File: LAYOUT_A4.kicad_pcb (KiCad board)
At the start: 2 copper layers, 209.6 x 205.7 mm, 108 parts, among them SW1 DPST, SW10 DPST, SW11 DPST, SW12 DPST, SW13 DPST, SW14 DPST, SW15 DPST, SW16 DPST, SW2 DPST, SW3 DPST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

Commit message: New A4 Layout
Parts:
- moved COLS1 160.2 mm to (174.0, 133.3)
- moved ROWS1 160.2 mm to (174.0, 120.7)
- moved C10 158.1 mm to (100.3, 146.1)
- moved C11 158.1 mm to (99.1, 170.2)
- moved C12 158.1 mm to (99.1, 236.2)
- moved C13 158.1 mm to (123.2, 146.1)
- moved C3 158.1 mm to (30.5, 236.2)
- moved C4 158.1 mm to (54.6, 146.1)
- moved C8 158.1 mm to (76.2, 170.2)
- moved C9 158.1 mm to (76.2, 236.2)
- moved COLS2 158.1 mm to (175.3, 172.7)
- moved D13 158.1 mm to (170.2, 257.8)
- moved D14 158.1 mm to (143.5, 261.6)
- moved D16 158.1 mm to (97.8, 261.6)
- moved D19 158.1 mm to (30.5, 229.9)
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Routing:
- net GND: track 0.00 -> 535.3 mm
- net /c1: track 0.00 -> 285.1 mm, vias 0 -> 1
- net /c2: track 0.00 -> 272.8 mm, vias 0 -> 2
- net /c4: track 0.00 -> 270.2 mm, vias 0 -> 3
- net /col2: track 0.00 -> 269.2 mm, vias 0 -> 4
- net /c3: track 0.00 -> 264.4 mm, vias 0 -> 3
- net /col1: track 0.00 -> 252.9 mm, vias 0 -> 2
- net /a4: track 0.00 -> 217.4 mm, vias 0 -> 1
- net /col3: track 0.00 -> 205.0 mm, vias 0 -> 2
- net /row3: track 0.00 -> 190.7 mm, vias 0 -> 2
- net /row1: track 0.00 -> 186.8 mm
- net /row2: track 0.00 -> 186.3 mm, vias 0 -> 1
- net /col4: track 0.00 -> 177.3 mm, vias 0 -> 2
- net /a1: track 0.00 -> 160.9 mm
- net /col5: track 0.00 -> 145.2 mm, vias 0 -> 2
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
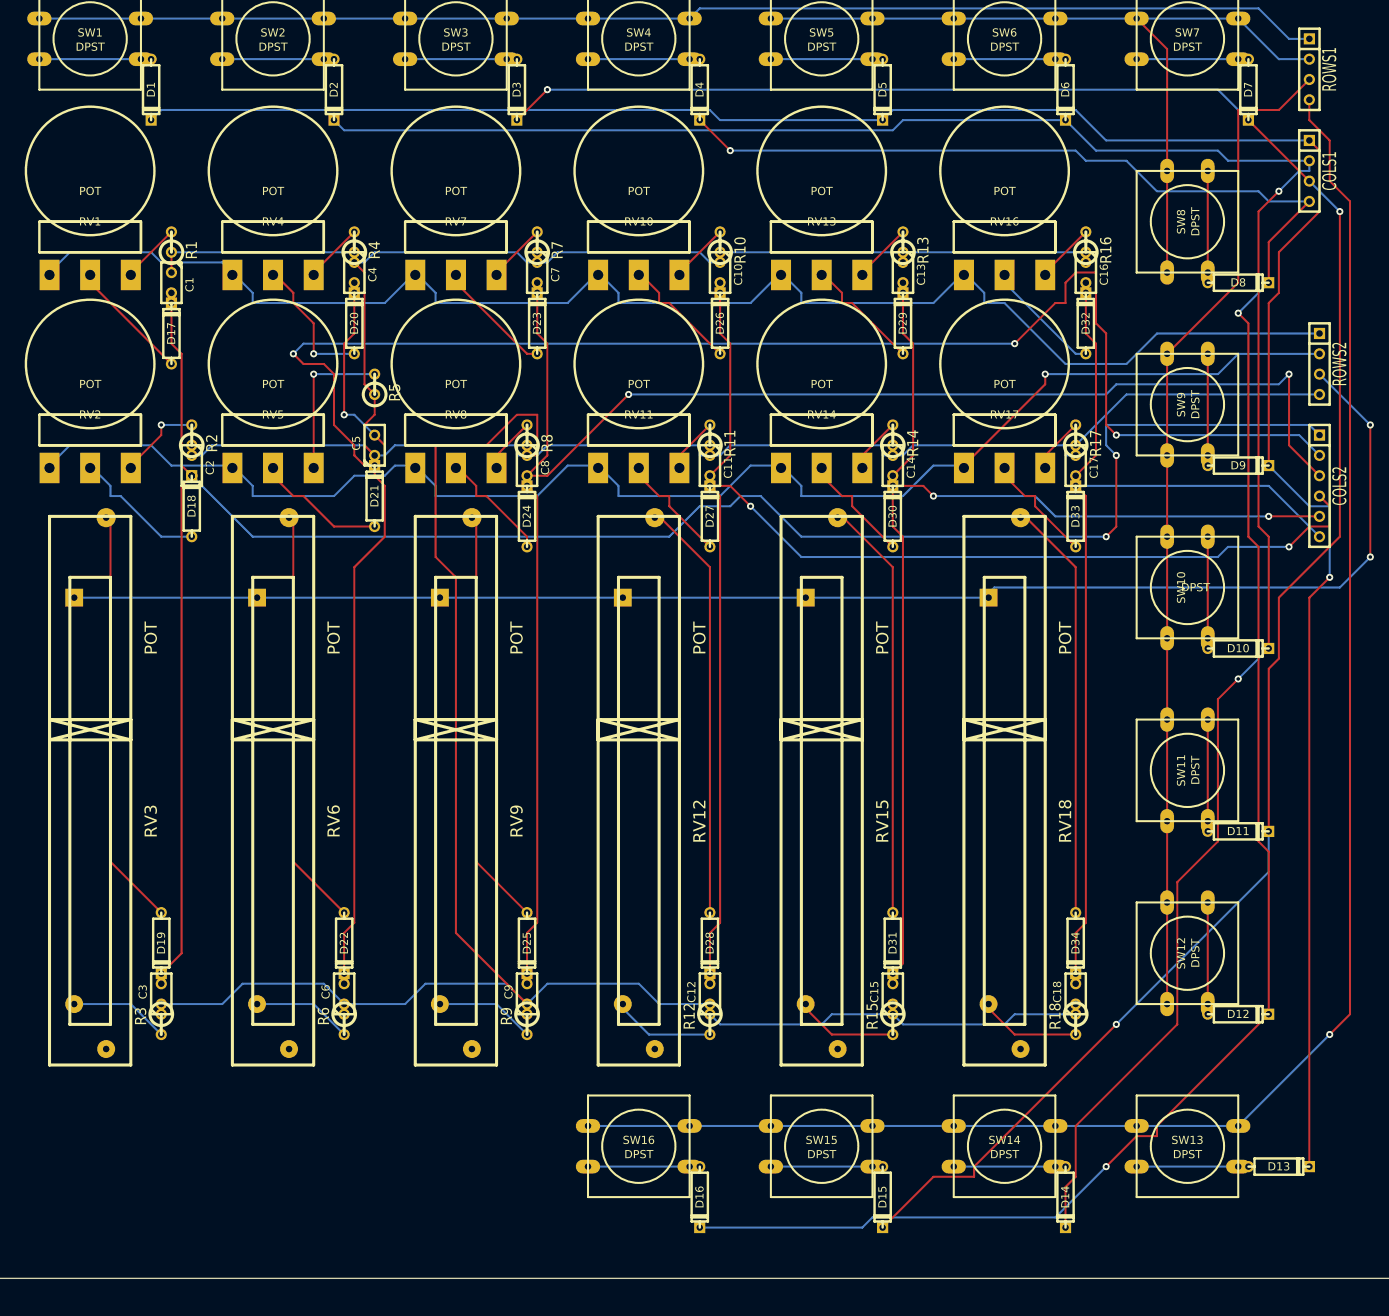
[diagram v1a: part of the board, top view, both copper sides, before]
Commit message: MIDI I/O added
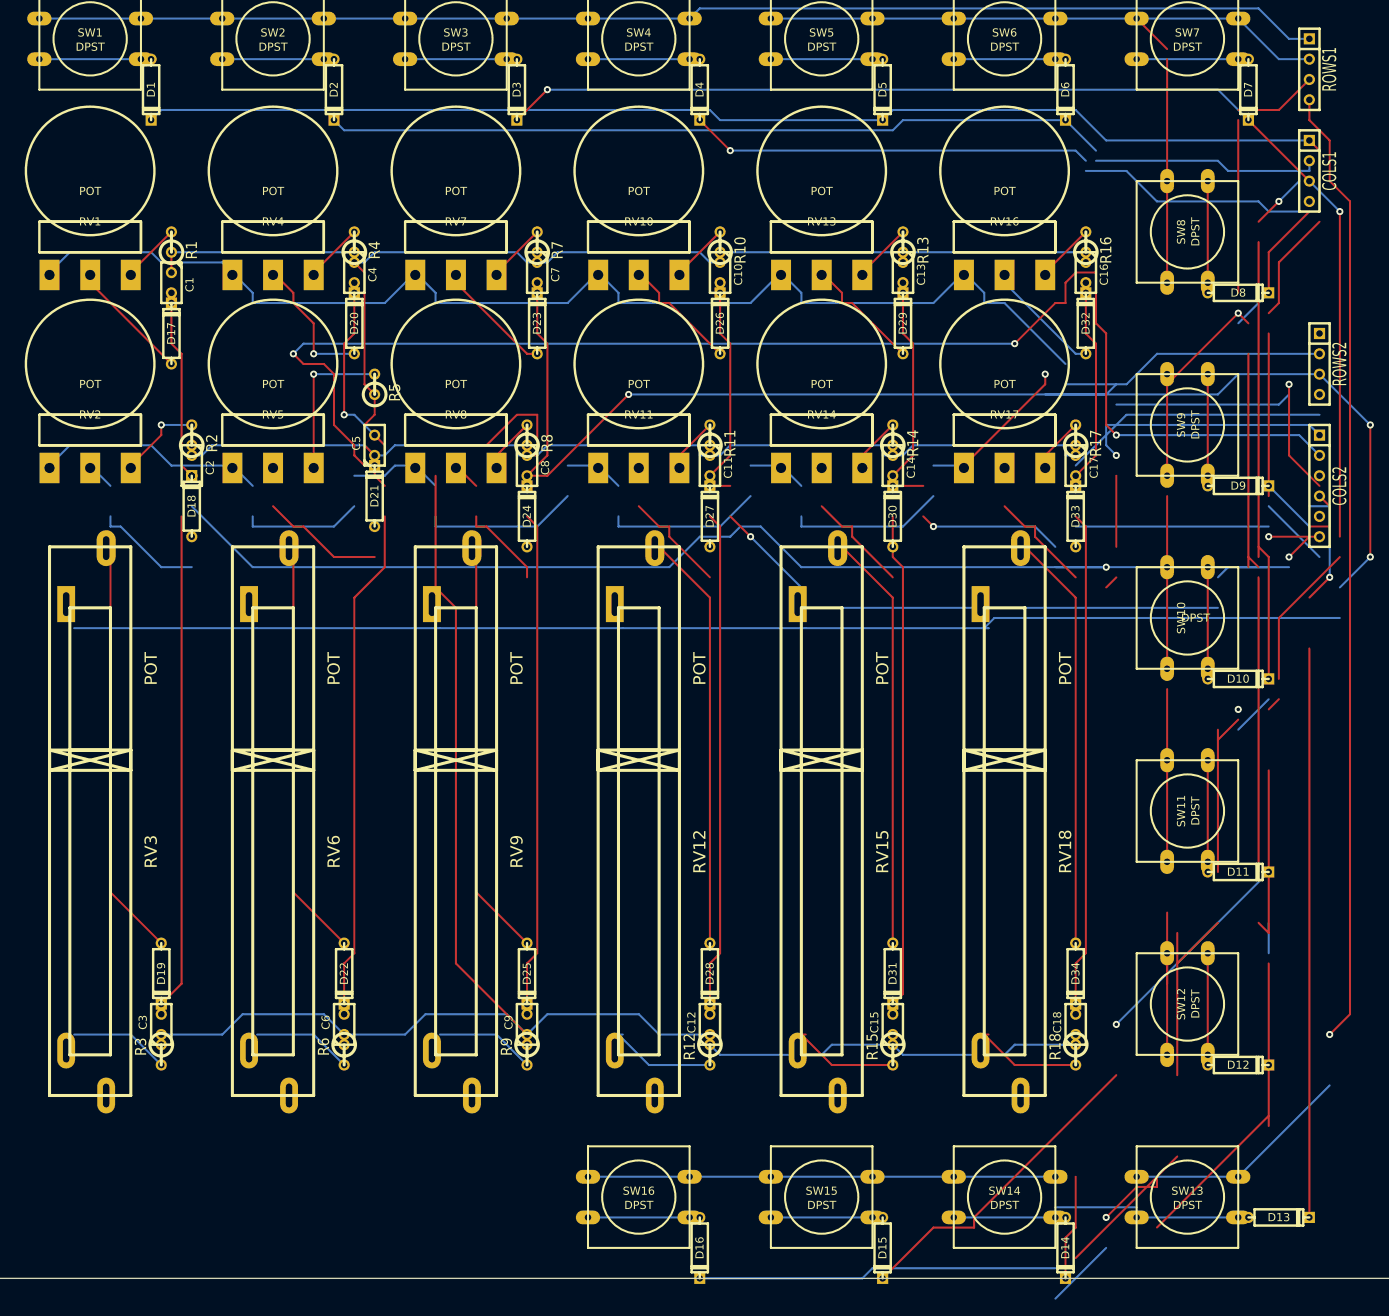
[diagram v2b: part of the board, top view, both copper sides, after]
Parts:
- moved D12 6.35 mm to (165.1, 245.1)
- moved D13 6.35 mm to (170.2, 264.2)
- moved D14 6.35 mm to (143.5, 268.0)
- moved D15 6.35 mm to (120.7, 268.0)
- moved D16 6.35 mm to (97.8, 268.0)
- moved SW12 6.35 mm to (158.8, 237.5)
- moved SW13 6.35 mm to (158.8, 261.6)
- moved SW14 6.35 mm to (135.9, 261.6)
- moved SW15 6.35 mm to (113.0, 261.6)
- moved SW16 6.35 mm to (90.2, 261.6)
- moved SW11 5.08 mm to (158.8, 213.4)
- moved D11 5.08 mm to (165.1, 221.0)
- moved C12 3.81 mm to (99.1, 240.0)
- moved C15 3.81 mm to (121.9, 240.0)
- moved C18 3.81 mm to (144.8, 240.0)
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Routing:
- net (no net): track 0.00 -> 1011.4 mm, vias 0 -> 8
- net /c4: track 270.2 -> 113.0 mm, vias 3 -> 1
- net /col1: track 252.9 -> 120.5 mm, vias 2 -> 1
- net /c2: track 272.8 -> 157.9 mm, vias 2 -> 0
- net GND: track 535.3 -> 440.1 mm
- net /col4: track 177.3 -> 99.7 mm, vias 2 -> 0
- net /row2: track 186.3 -> 111.2 mm
- net /col5: track 145.2 -> 94.1 mm, vias 2 -> 0
- net /c1: track 285.1 -> 235.7 mm, vias 1 -> 0
- net /c3: track 264.4 -> 218.8 mm
- net /col3: track 205.0 -> 168.7 mm, vias 2 -> 1
- net /row1: track 186.8 -> 153.5 mm
- net /a3: track 125.9 -> 96.0 mm, vias 0 -> 1
- net /col6: track 123.4 -> 96.6 mm, vias 0 -> 1
- net N-0000067: track 16.3 -> 0.97 mm
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
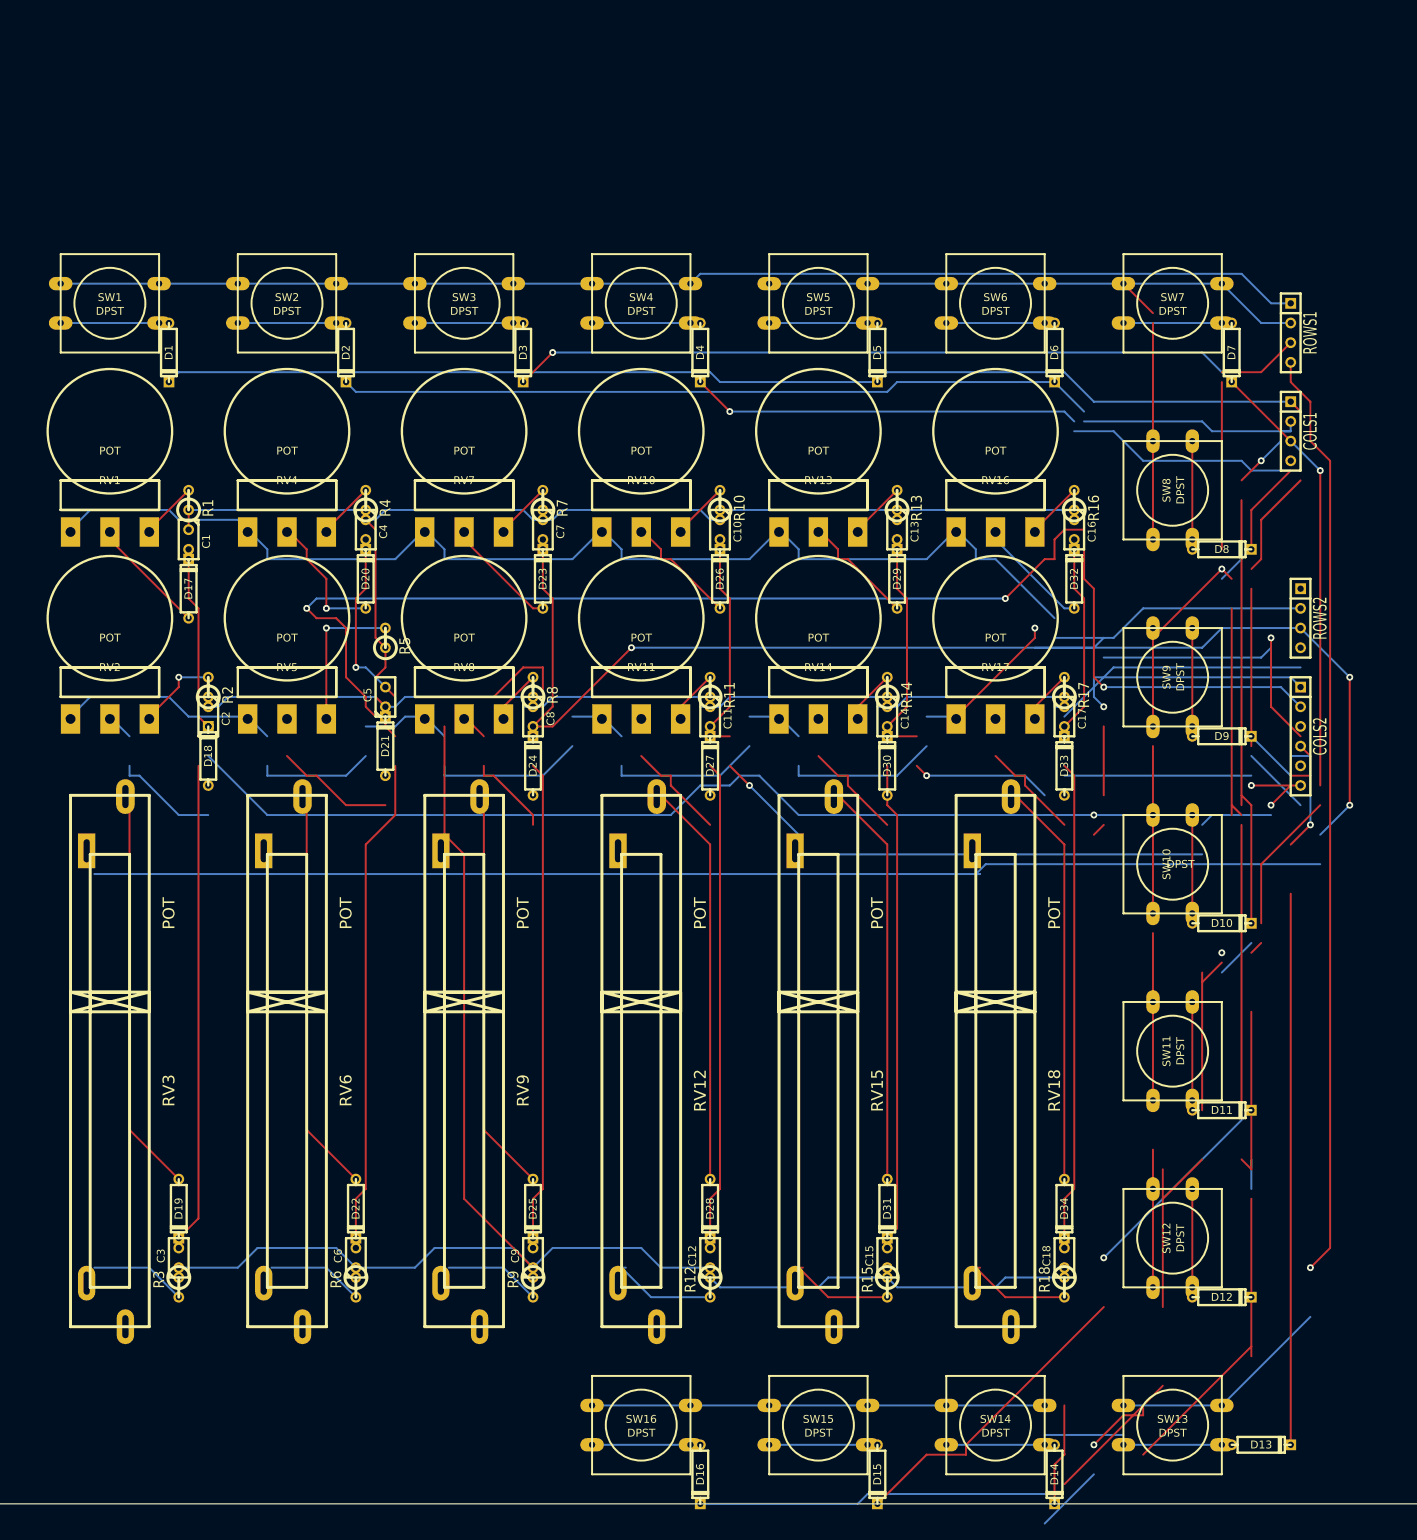
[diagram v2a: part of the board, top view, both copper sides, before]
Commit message: Fixed spacing errors
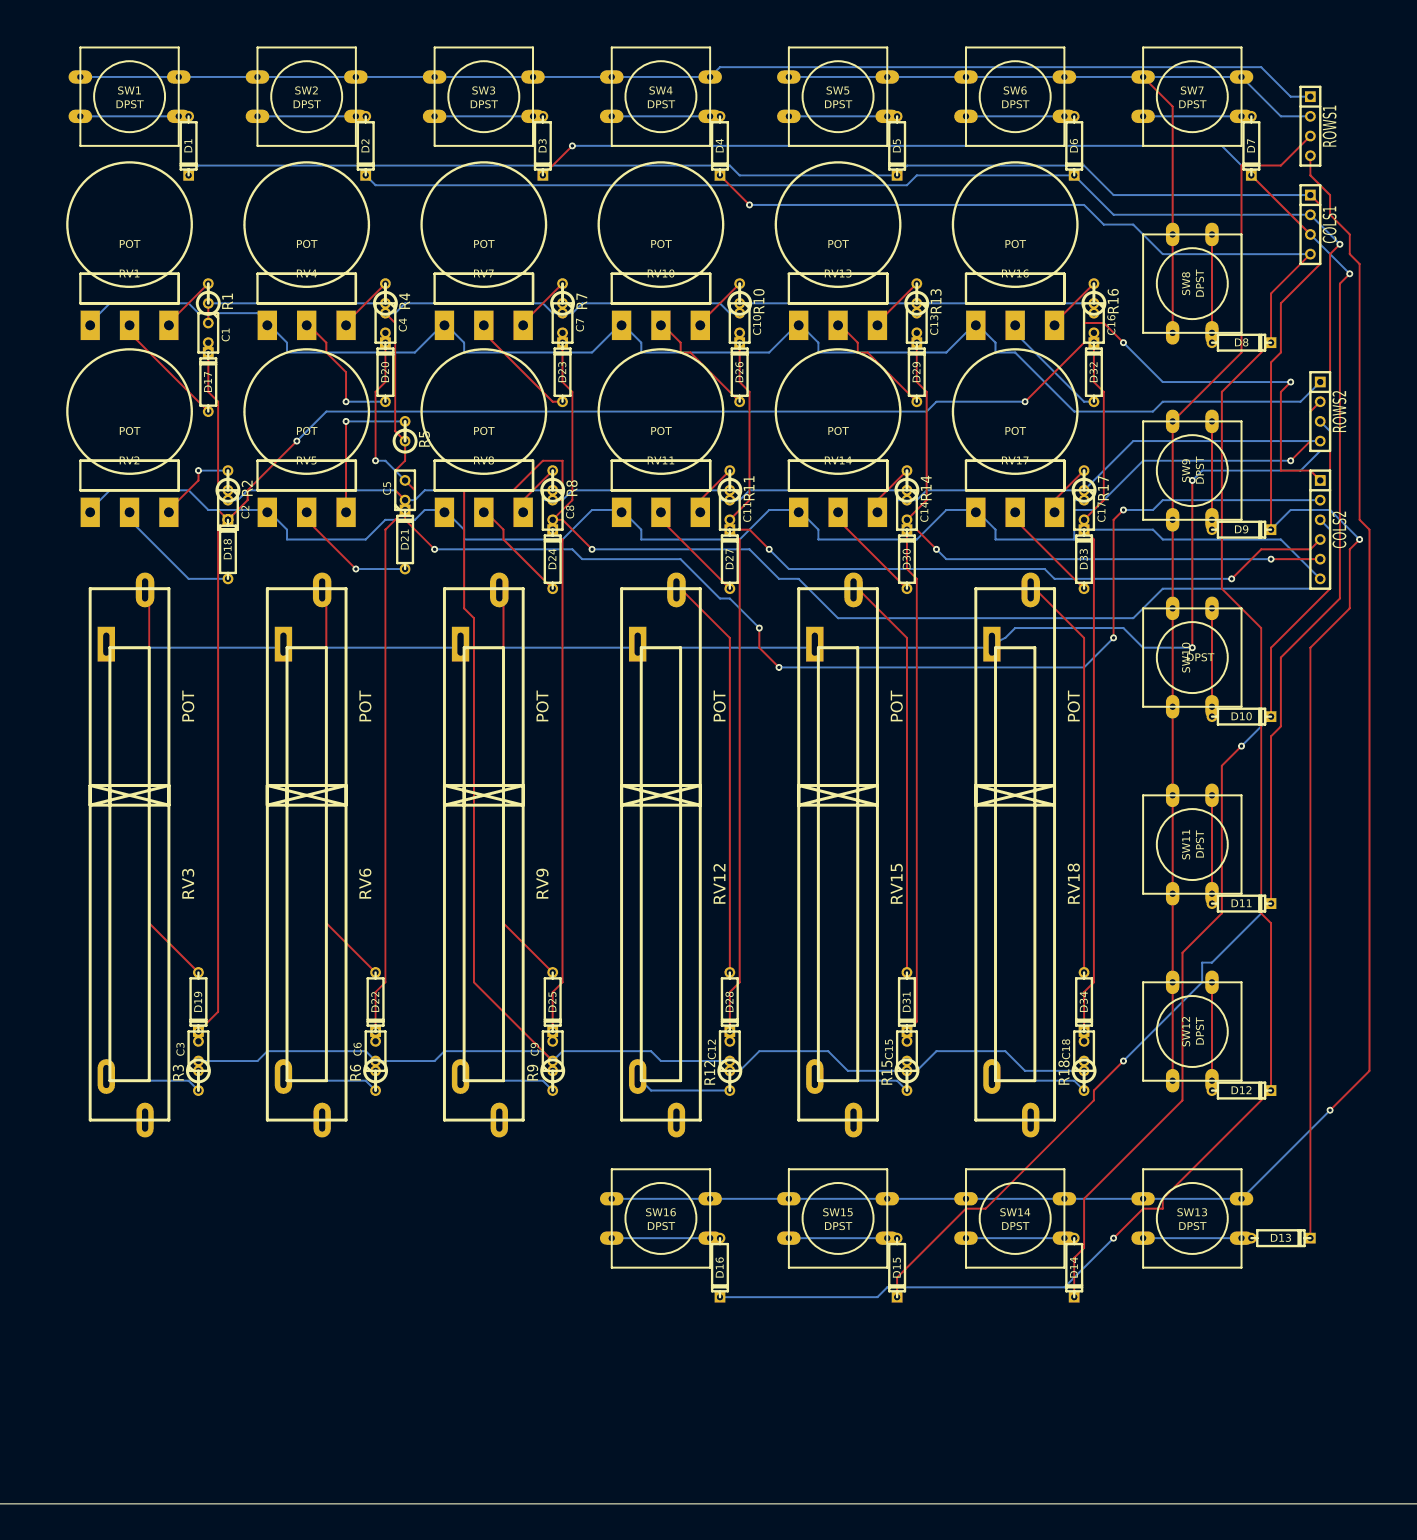
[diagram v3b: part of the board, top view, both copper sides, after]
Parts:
- moved D14 26.8 mm to (146.1, 241.3)
- moved RV16 26.8 mm to (138.4, 119.4)
- moved RV17 26.8 mm to (138.4, 143.5)
- moved RV18 26.8 mm to (138.4, 186.7)
- moved SW14 26.8 mm to (138.4, 234.9)
- moved C10 26.8 mm to (102.9, 119.4)
- moved C11 26.8 mm to (101.6, 143.5)
- moved C13 26.8 mm to (125.7, 119.4)
- moved C14 26.8 mm to (124.5, 143.5)
- moved C16 26.8 mm to (148.6, 119.4)
- moved C17 26.8 mm to (147.3, 143.5)
- moved C2 26.8 mm to (36.8, 143.5)
- moved C4 26.8 mm to (57.1, 119.4)
- moved C7 26.8 mm to (80.0, 119.4)
- moved C8 26.8 mm to (78.7, 143.5)
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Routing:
- net (no net): track 1011.4 -> 0.00 mm, vias 8 -> 0
- net /c4: track 113.0 -> 278.6 mm, vias 1 -> 2
- net /col1: track 120.5 -> 263.4 mm, vias 1 -> 4
- net /c2: track 157.9 -> 280.6 mm, vias 0 -> 2
- net GND: track 440.1 -> 538.0 mm
- net /row2: track 111.2 -> 193.9 mm
- net /col4: track 99.7 -> 175.0 mm, vias 0 -> 2
- net /c1: track 235.7 -> 301.1 mm, vias 0 -> 1
- net /col5: track 94.1 -> 149.0 mm, vias 0 -> 2
- net /c3: track 218.8 -> 271.1 mm
- net /col3: track 168.7 -> 210.7 mm
- net /a3: track 96.0 -> 132.3 mm, vias 1 -> 0
- net /row1: track 153.5 -> 186.8 mm
- net /col6: track 96.6 -> 127.2 mm, vias 1 -> 0
- net /col2: track 269.2 -> 244.3 mm, vias 4 -> 6
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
